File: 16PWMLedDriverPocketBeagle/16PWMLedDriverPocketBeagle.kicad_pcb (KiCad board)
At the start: 2 copper layers, 97.8 x 128.3 mm, 43 parts, among them J1 RJ45, J2 RJ45, P1 POCKETBEAGLE-P1, P2 POCKETBEAGLE-P2, P3 C A0 A1 A2 A3 A4 A5 A6 A7, P4 C B0 B1 B2 B3 B4 B5 B6 B7, T1 + 15 in -, T2 + 15 out -, U1 TCAN332DR, U2 SN65HVD233-HT, U3 LM2574N-5.0, U4 PCA9685, U5 TBD62X83A, U6 TBD62X83A

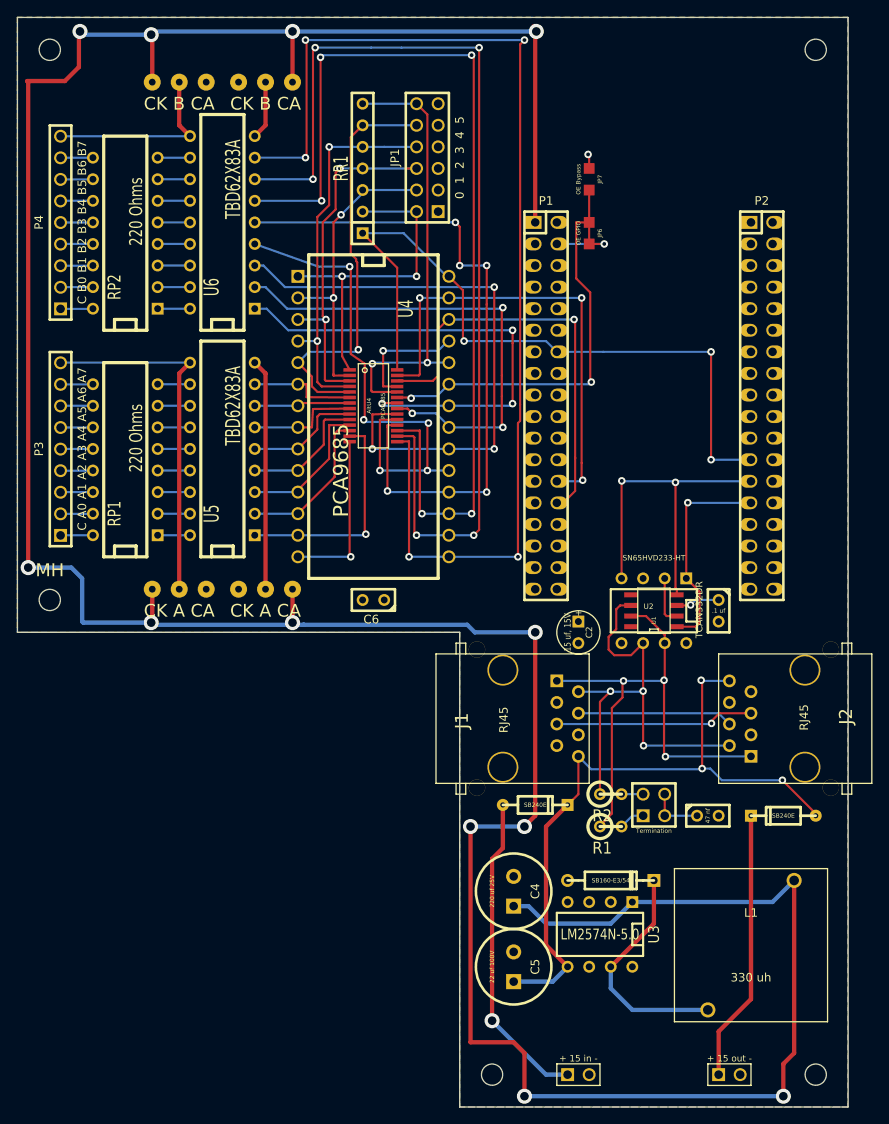
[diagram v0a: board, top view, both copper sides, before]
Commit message: Convert the 16PWM Led Drivers to use 12V for the LEDs.
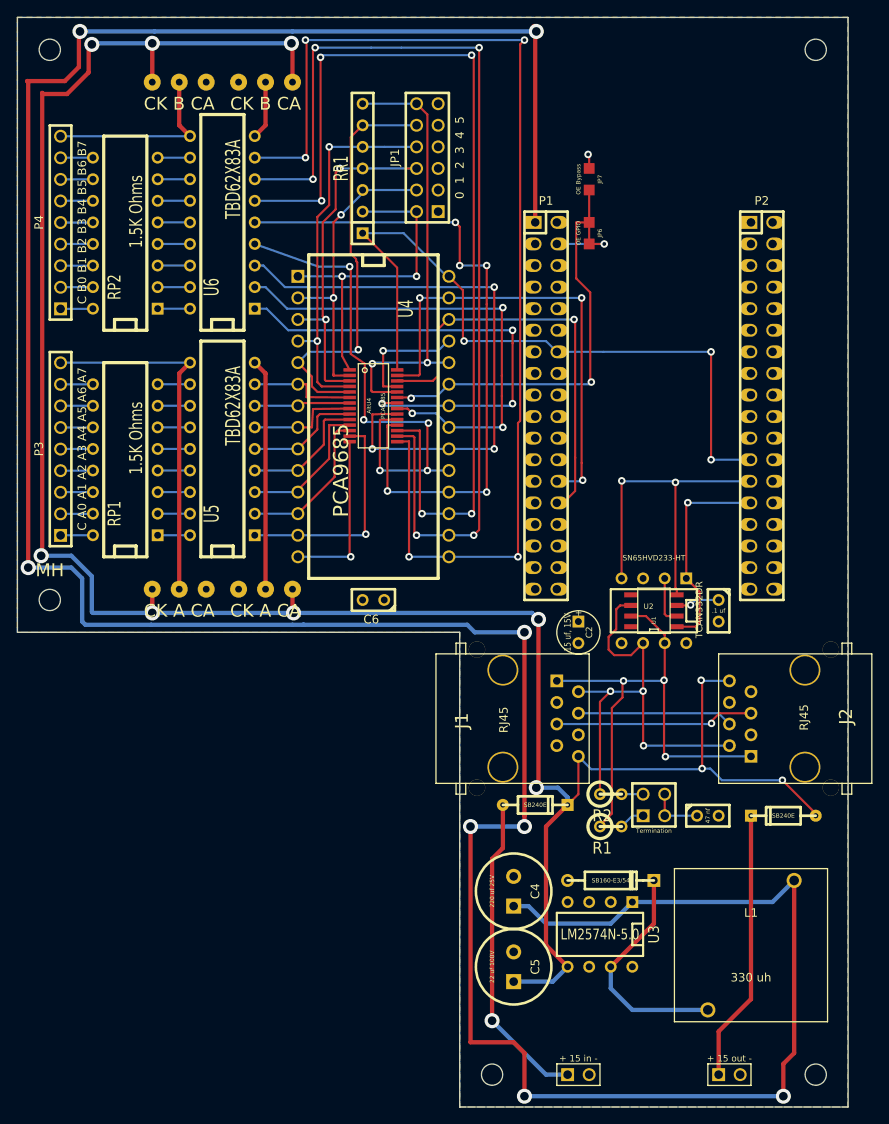
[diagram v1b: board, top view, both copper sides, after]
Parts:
- RP1, RP2: value 220 Ohms -> 1.5K Ohms
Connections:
- C5 pad 1: /Power Supply/12-15 Volt input -> +12V
- D1 pad 2: /Power Supply/12-15 Volt input -> +12V
- D2 pad 1: /Power Supply/12-15 Volt input -> +12V
- J1 pad 8: /Power Supply/12-15 Volt input -> +12V
- J2 pad 8: /Power Supply/12-15 Volt input -> +12V
- JP2 pad 1: +5V -> +12V
- JP3 pad 3: +5V -> +12V
- JP4 pad 1: +5V -> +12V
- JP5 pad 3: +5V -> +12V
- U3 pad 5: /Power Supply/12-15 Volt input -> +12V
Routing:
- net +12V: track 0.00 -> 271.3 mm, vias 0 -> 11
- net /Power Supply/12-15 Volt input: track 79.3 -> 0.00 mm, vias 3 -> 0
- net +5V: track 392.7 -> 370.1 mm, vias 12 -> 8

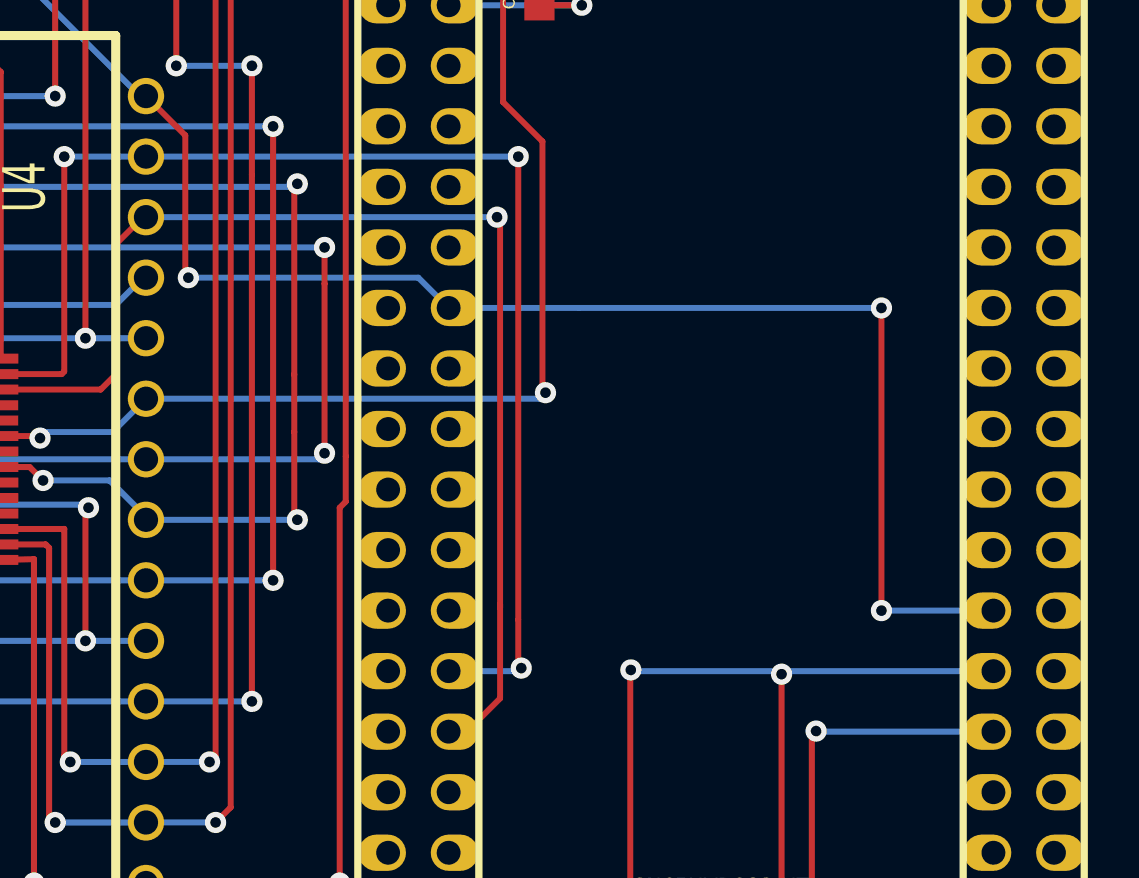
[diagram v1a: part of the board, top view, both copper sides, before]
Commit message: Move Pocket Beagle SDA usage from I2C2 to I2C1 (reserved I2C for eeprom?).
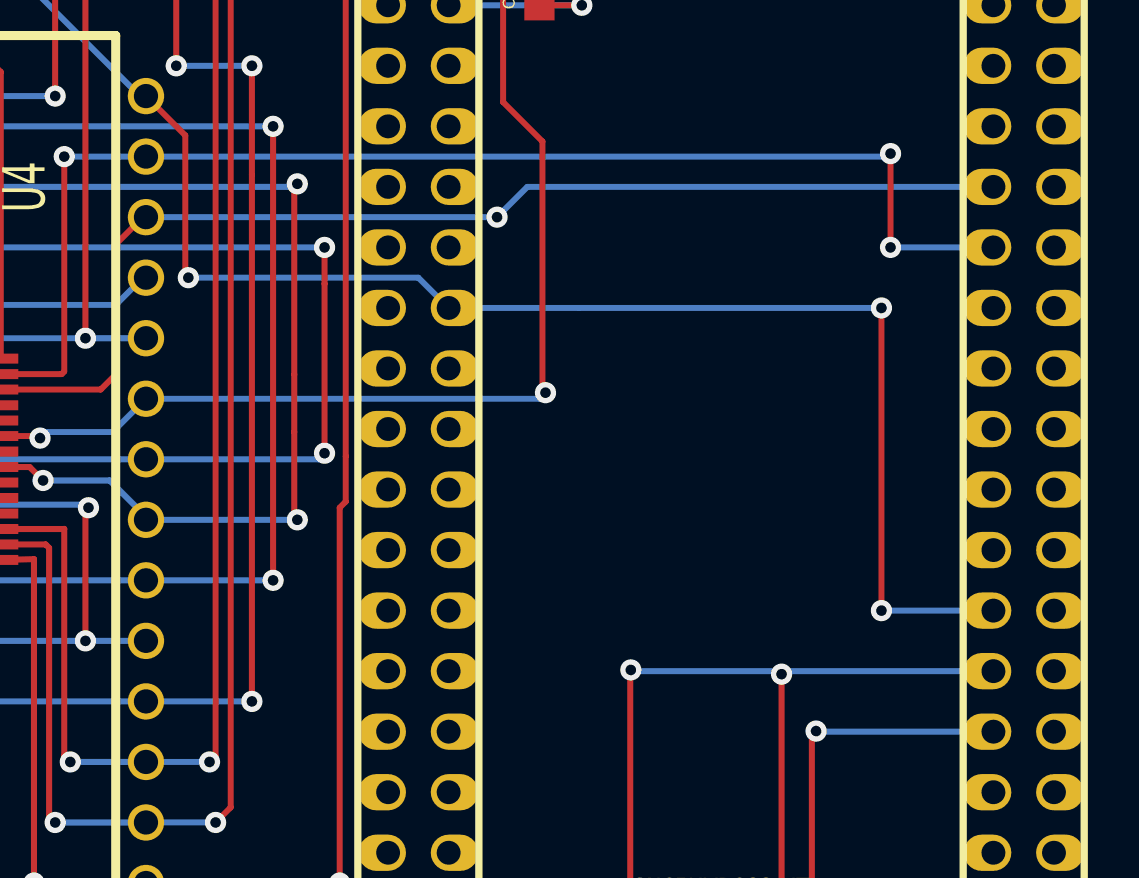
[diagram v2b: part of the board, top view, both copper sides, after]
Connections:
- P1 pad 26: /PCA9685 Driver/SDA -> (no net)
- P1 pad 28: /PCA9685 Driver/SCL -> (no net)
- P2 pad 11: (no net) -> /PCA9685 Driver/SDA
- P2 pad 9: (no net) -> /PCA9685 Driver/SCL
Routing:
- net /PCA9685 Driver/SCL: track 50.1 -> 48.6 mm
- net /PCA9685 Driver/SDA: track 56.2 -> 54.7 mm
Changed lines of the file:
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@@
     (thickness 1.6)
     (drawings 7)
-    (tracks 607)
+    (tracks 601)
     (zones 0)
     (modules 43)
@@
   )
   (setup
-    (last_trace_width 0.508)
+    (last_trace_width 0.25)
     (user_trace_width 0.508)
     (user_trace_width 0.889)
@@
     (pad 26 thru_hole oval (at 8.89 -1.27 270) (size 1.524 1.99898) (drill 1.00076 (offset 0 -0.24892))
       (layers *.Cu *.Mask F.SilkS)
-      (net 10 "/PCA9685 Driver/SDA")
     )
     (pad 27 thru_hole oval (at 11.43 1.27 270) (size 1.524 1.99898) (drill 1.00076 (offset 0 0.24892))
@@
     (pad 28 thru_hole oval (at 11.43 -1.27 270) (size 1.524 1.99898) (drill 1.00076 (offset 0 -0.24892))
       (layers *.Cu *.Mask F.SilkS)
-      (net 9 "/PCA9685 Driver/SCL")
     )
     (pad 29 thru_hole oval (at 13.97 1.27 270) (size 1.524 1.99898) (drill 1.00076 (offset 0 0.24892))
@@
     (pad 9 thru_hole oval (at -11.43 1.27 270) (size 1.524 1.99898) (drill 1.00076 (offset 0 0.24892))
       (layers *.Cu *.Mask F.SilkS)
+      (net 9 "/PCA9685 Driver/SCL")
     )
     (pad 10 thru_hole oval (at -11.43 -1.27 270) (size 1.524 1.99898) (drill 1.00076 (offset 0 -0.24892))
@@
     (pad 11 thru_hole oval (at -8.89 1.27 270) (size 1.524 1.99898) (drill 1.00076 (offset 0 0.24892))
       (layers *.Cu *.Mask F.SilkS)
+      (net 10 "/PCA9685 Driver/SDA")
     )
     (pad 12 thru_hole oval (at -8.89 -1.27 270) (size 1.524 1.99898) (drill 1.00076 (offset 0 -0.24892))
@@
   (segment (start 135.128 83.82) (end 133.35 83.82) (width 0.25) (layer F.Cu) (net 8))
   (via (at 135.128 83.82) (size 0.889) (layers F.Cu B.Cu) (net 8))
-  (segment (start 131.699 108.966) (end 131.699 112.903) (width 0.25) (layer F.Cu) (net 9))
-  (segment (start 130.302 114.3) (end 129.54 114.3) (width 0.25) (layer F.Cu) (net 9))
-  (segment (start 131.699 112.903) (end 130.302 114.3) (width 0.25) (layer F.Cu) (net 9))
+  (segment (start 152.4 91.44) (end 132.842 91.44) (width 0.25) (layer B.Cu) (net 9))
+  (segment (start 132.842 91.44) (end 131.572 92.71) (width 0.25) (layer B.Cu) (net 9))
   (segment (start 116.84 92.71) (end 131.572 92.71) (width 0.25) (layer B.Cu) (net 9))
-  (segment (start 131.699 92.837) (end 131.699 108.966) (width 0.25) (layer F.Cu) (net 9))
-  (segment (start 131.699 108.966) (end 131.699 109.093) (width 0.25) (layer F.Cu) (net 9))
   (segment (start 131.572 92.71) (end 131.699 92.837) (width 0.25) (layer F.Cu) (net 9))
   (via (at 131.572 92.71) (size 0.889) (layers F.Cu B.Cu) (net 9))
@@
   (segment (start 115.57 99.314) (end 115.57 93.853) (width 0.25) (layer F.Cu) (net 9))
   (segment (start 114.94008 99.94392) (end 115.57 99.314) (width 0.25) (layer F.Cu) (net 9))
-  (segment (start 132.461 109.601) (end 132.461 111.506) (width 0.25) (layer F.Cu) (net 10))
-  (segment (start 132.461 109.601) (end 132.461 90.17) (width 0.25) (layer F.Cu) (net 10))
-  (via (at 132.461 90.17) (size 0.889) (layers F.Cu B.Cu) (net 10))
-  (segment (start 116.84 90.17) (end 132.461 90.17) (width 0.25) (layer B.Cu) (net 10))
-  (segment (start 132.461 111.76) (end 129.54 111.76) (width 0.25) (layer B.Cu) (net 10))
-  (segment (start 132.588 111.633) (end 132.461 111.76) (width 0.25) (layer B.Cu) (net 10))
-  (via (at 132.588 111.633) (size 0.889) (layers F.Cu B.Cu) (net 10))
-  (segment (start 132.461 111.506) (end 132.588 111.633) (width 0.25) (layer F.Cu) (net 10))
-  (segment (start 129.54 111.76) (end 130.302 111.76) (width 0.25) (layer F.Cu) (net 10))
+  (segment (start 116.84 90.17) (end 147.955 90.17) (width 0.25) (layer B.Cu) (net 10))
+  (segment (start 148.082 93.98) (end 152.4 93.98) (width 0.25) (layer B.Cu) (net 10))
+  (via (at 148.082 93.98) (size 0.889) (layers F.Cu B.Cu) (net 10))
+  (segment (start 148.082 90.043) (end 148.082 93.98) (width 0.25) (layer F.Cu) (net 10))
+  (via (at 148.082 90.043) (size 0.889) (layers F.Cu B.Cu) (net 10))
+  (segment (start 147.955 90.17) (end 148.082 90.043) (width 0.25) (layer B.Cu) (net 10))
   (segment (start 110.74908 99.29622) (end 113.30178 99.29622) (width 0.25) (layer F.Cu) (net 10))
   (segment (start 113.411 90.17) (end 116.84 90.17) (width 0.25) (layer B.Cu) (net 10))

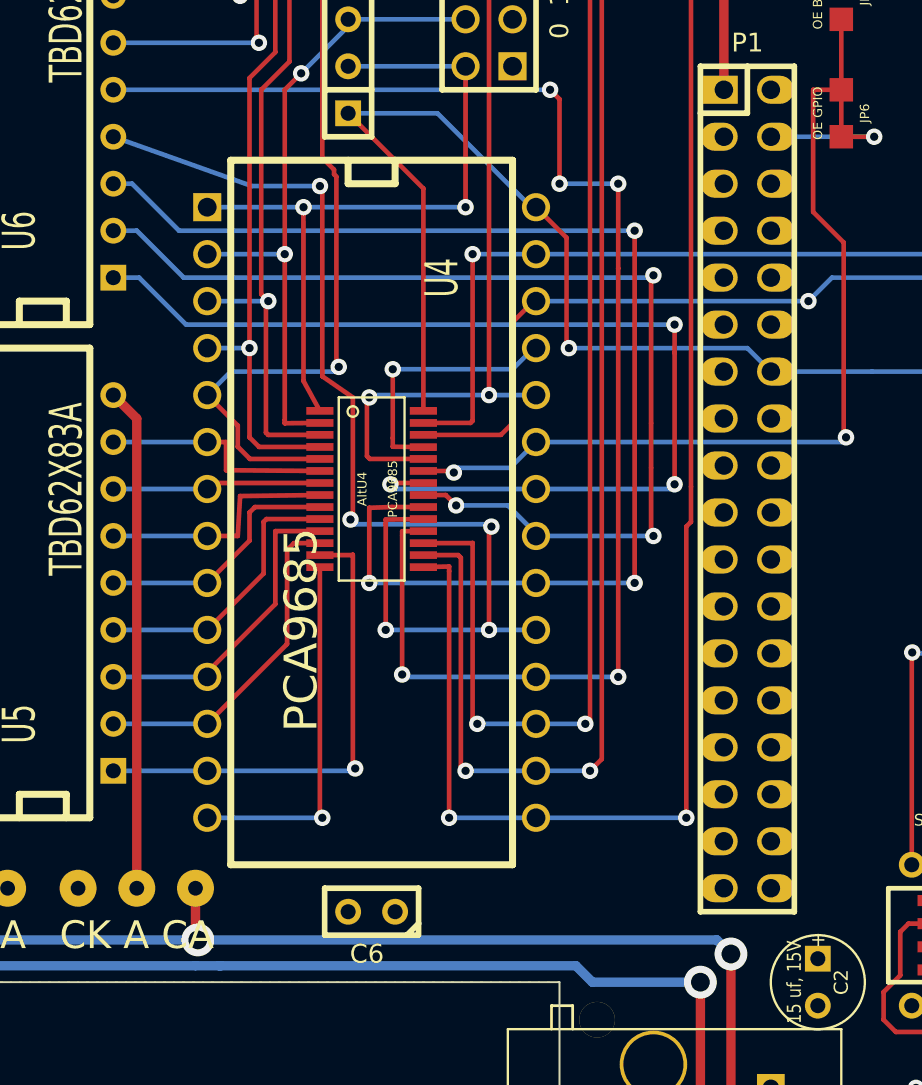
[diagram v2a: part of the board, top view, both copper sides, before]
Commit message: Remove unused DIP and add LED power terminals.
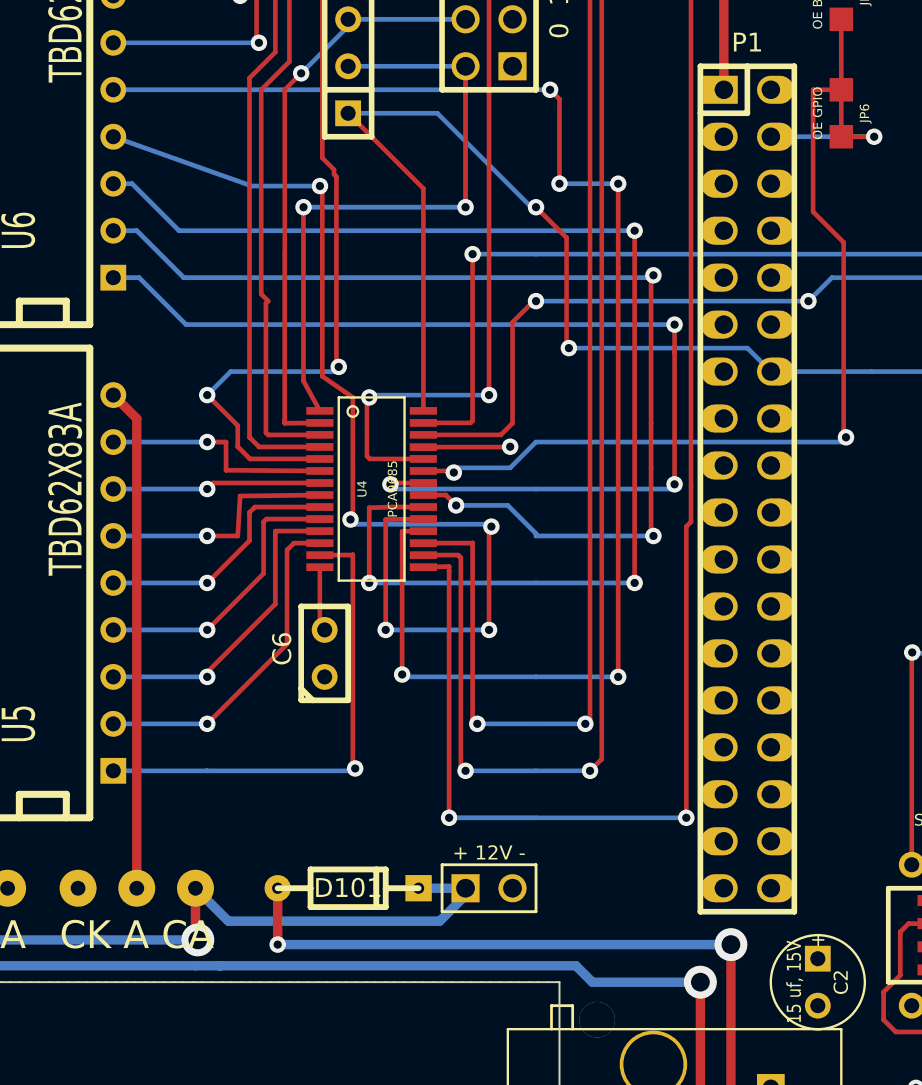
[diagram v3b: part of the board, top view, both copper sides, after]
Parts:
- removed AltU4: PCA9685, tssop-28
- added D101: SB240E, DO-35, F.Cu at (106.7, 124.5)
- added T101: + 12V -, ScrewTerm2.54-2, F.Cu at (114.3, 124.5)
- U4: footprint DIP-28__700 -> tssop-28
- moved C6 14.2 mm to (105.4, 111.8), turned to 90 degrees
- moved U4 1.27 mm to (108.0, 102.9)
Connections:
- C5 pad 1: +12V -> /Power Supply/12-15 Volt input
- D1 pad 2: +12V -> /Power Supply/12-15 Volt input
- D2 pad 1: +12V -> /Power Supply/12-15 Volt input
- J1 pad 8: +12V -> /Power Supply/12-15 Volt input
- J2 pad 8: +12V -> /Power Supply/12-15 Volt input
- U3 pad 5: +12V -> /Power Supply/12-15 Volt input
- U4 pad 25: N-00000120 (its old number) -> GND
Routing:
- net /Power Supply/12-15 Volt input: track 0.00 -> 132.4 mm, vias 0 -> 6
- net +12V: track 271.3 -> 156.7 mm, vias 11 -> 6
- net N-00000120 (its old number): track 14.1 -> 0.00 mm, vias 1 -> 0
- net GND: track 27.3 -> 15.8 mm
- net N-00000129: track 39.2 -> 34.0 mm
- net N-00000123: track 35.7 -> 31.5 mm, vias 2 -> 1
- net N-00000124: track 42.5 -> 39.2 mm, vias 2 -> 1
- net N-00000127: track 52.8 -> 50.2 mm
- net N-00000121: track 60.7 -> 58.2 mm
- net N-00000125: track 44.9 -> 42.6 mm, vias 2 -> 1
- net N-00000126: vias 1 -> 2
- net N-00000115: vias 0 -> 1
- net N-00000118: vias 0 -> 1
- net N-00000114: vias 0 -> 1
- net N-00000113: vias 0 -> 1
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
